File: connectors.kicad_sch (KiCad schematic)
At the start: 7 parts, among them J2 217183-0001, J3 BM03B-SRSS-TB

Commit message: test points
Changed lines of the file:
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@@
+    (stroke (width 0) (type default))
+  )
+  (wire (pts (xy 213.36 110.49) (xy 220.98 110.49))
     (stroke (width 0) (type default))
   )
@@
     (stroke (width 0) (type default))
   )
-  (wire (pts (xy 213.36 105.41) (xy 222.25 105.41))
-    (stroke (width 0) (type default))
-  )
-  (wire (pts (xy 213.36 110.49) (xy 222.25 110.49))
+  (wire (pts (xy 213.36 105.41) (xy 220.98 105.41))
     (stroke (width 0) (type default))
   )
@@
   )
   (text_box "follows Raspberry Pi 3-pin Debug Connector Specification (SWD)"
-    (at 198.755 91.44 0) (size 21.59 10.16)
+    (at 194.31 91.44 0) (size 21.59 10.16)
     (stroke (width 0) (type default) (color 132 0 0 1))
     (fill (type color) (color 255 255 194 1))
@@
   )
   (text_box ""
-    (at 186.69 87.63 0) (size 46.99 38.1)
+    (at 186.69 87.63 0) (size 45.72 38.1)
     (stroke (width 0) (type dash) (color 132 0 0 1))
     (fill (type none))
@@
     (effects (font (size 2 2) (thickness 0.4) bold italic (color 132 0 0 1)) (justify left bottom))
   )
-  (hierarchical_label "SWD" (shape bidirectional) (at 222.25 110.49 0) (fields_autoplaced)
+  (hierarchical_label "SWD" (shape bidirectional) (at 220.98 110.49 0) (fields_autoplaced)
     (effects (font (size 1.27 1.27)) (justify left))
   )
@@
     (effects (font (size 1.27 1.27)) (justify left))
   )
-  (hierarchical_label "SWCLK" (shape input) (at 222.25 105.41 0) (fields_autoplaced)
+  (hierarchical_label "SWCLK" (shape input) (at 220.98 105.41 0) (fields_autoplaced)
     (effects (font (size 1.27 1.27)) (justify left))
   )

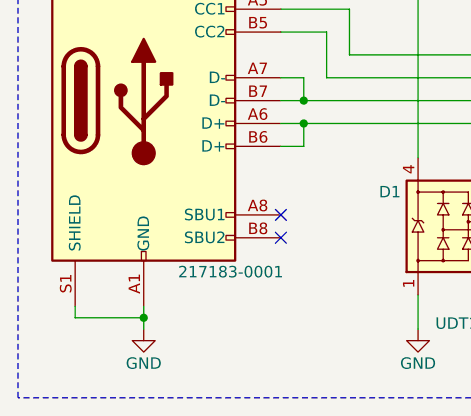
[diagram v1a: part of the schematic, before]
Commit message: finish new mouse button design
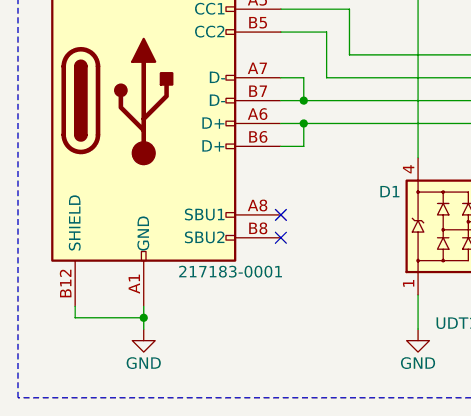
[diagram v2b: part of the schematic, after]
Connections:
- net GND: no longer J2.S1 (SHIELD)
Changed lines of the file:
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@@
     (pin "B4")
     (pin "B7")
-    (pin "S1")
+    (pin "B12")
     (instances
       (project "gkos_pebble"

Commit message: in progress pcb
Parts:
- C1: footprint Capacitor_SMD:C_0805_2012Metric -> Capacitor_SMD:C_0603_1608Metric
- R1, R2: footprint Resistor_SMD:R_0805_2012Metric -> Resistor_SMD:R_0603_1608Metric
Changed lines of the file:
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@@
       (effects (font (size 1.27 1.27)) (justify right))
     )
-    (property "Footprint" "Resistor_SMD:R_0805_2012Metric" (at 141.732 121.92 90)
+    (property "Footprint" "Resistor_SMD:R_0603_1608Metric" (at 141.732 121.92 90)
       (effects (font (size 1.27 1.27)) hide)
     )
@@
       (effects (font (size 1.27 1.27)) (justify right))
     )
-    (property "Footprint" "Resistor_SMD:R_0805_2012Metric" (at 132.842 121.92 90)
+    (property "Footprint" "Resistor_SMD:R_0603_1608Metric" (at 132.842 121.92 90)
       (effects (font (size 1.27 1.27)) hide)
     )
@@
       (effects (font (size 1.27 1.27)) (justify right))
     )
-    (property "Footprint" "Capacitor_SMD:C_0805_2012Metric" (at 155.9052 95.25 0)
-      (effects (font (size 1.27 1.27)) hide)
-    )
+    (property "Footprint" "Capacitor_SMD:C_0603_1608Metric" (at 155.9052 95.25 0)
+      (effects (font (size 1.27 1.27)) hide)
+    )
